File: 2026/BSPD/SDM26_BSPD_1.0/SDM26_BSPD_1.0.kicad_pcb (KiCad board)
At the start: 2 copper layers, 10 parts, among them Q1 2N7002,215, Q2 2N7002,215

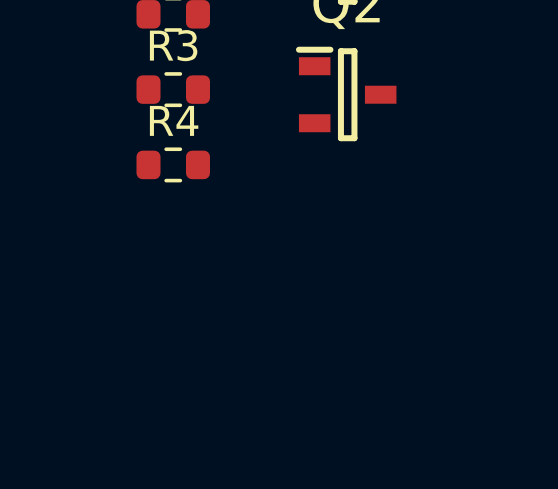
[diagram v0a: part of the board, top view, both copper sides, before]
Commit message: BSPD logic and latch simulated in Falstad
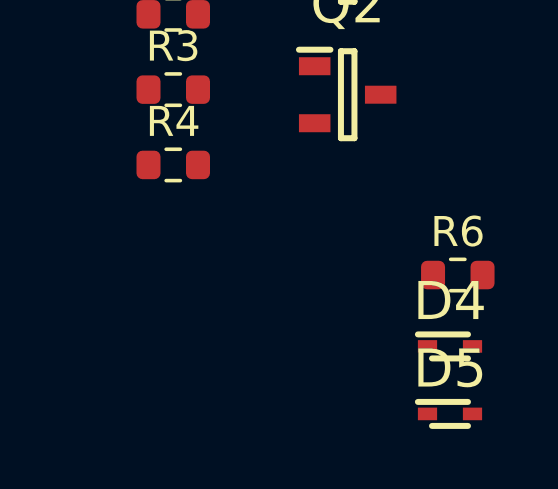
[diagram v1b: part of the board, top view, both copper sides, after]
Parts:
- added D4: BAT54XV2T1G, SDM_MiscFootprint:SODFL1608X70N, F.Cu at (125.5, 93.8)
- added D5: BAT54XV2T1G, SDM_MiscFootprint:SODFL1608X70N, F.Cu at (125.5, 96.0)
- added R6: 1k, Resistor_SMD:R_0603_1608Metric, F.Cu at (125.8, 91.4)
- D1, D2: footprint SDM_DIODE:SODFL1608X70N -> SDM_MiscFootprint:SODFL1608X70N
- D3: footprint SDM_SCR:SOT230P700X190-4N -> SDM_MiscFootprint:SOT230P700X190-4N
- Q1: footprint SDM_MOSFET_N-CHANNEL:SOT95P230X110-3N -> SDM_MiscFootprint:SOT95P230X110-3N
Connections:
- D1 pad 1: Net-(D1-K) -> /SCR Gate
- D3 pad 1: GND -> (no net)
- D3 pad 2: BSPD SIGNAL OUT -> (no net)
- D3 pad 3: Net-(D1-K) -> (no net)
- D3 pad 4: BSPD SIGNAL OUT -> (no net)
- Q1 pad 1: /12V MASTER -> (no net)
- Q1 pad 2: GND -> (no net)
- Q1 pad 3: Net-(D1-A) -> (no net)
- R1 pad 1: Net-(D1-A) -> /12V IGNITION
- R1 pad 2: /12V IGNITION -> Net-(D1-A)
- R2 pad 1: Net-(D1-K) -> /SCR Gate
- R4 pad 1: /12V IGNITION -> Net-(D4-K)
- R4 pad 2: BSPD SIGNAL OUT -> BSPD KILL SIGNAL

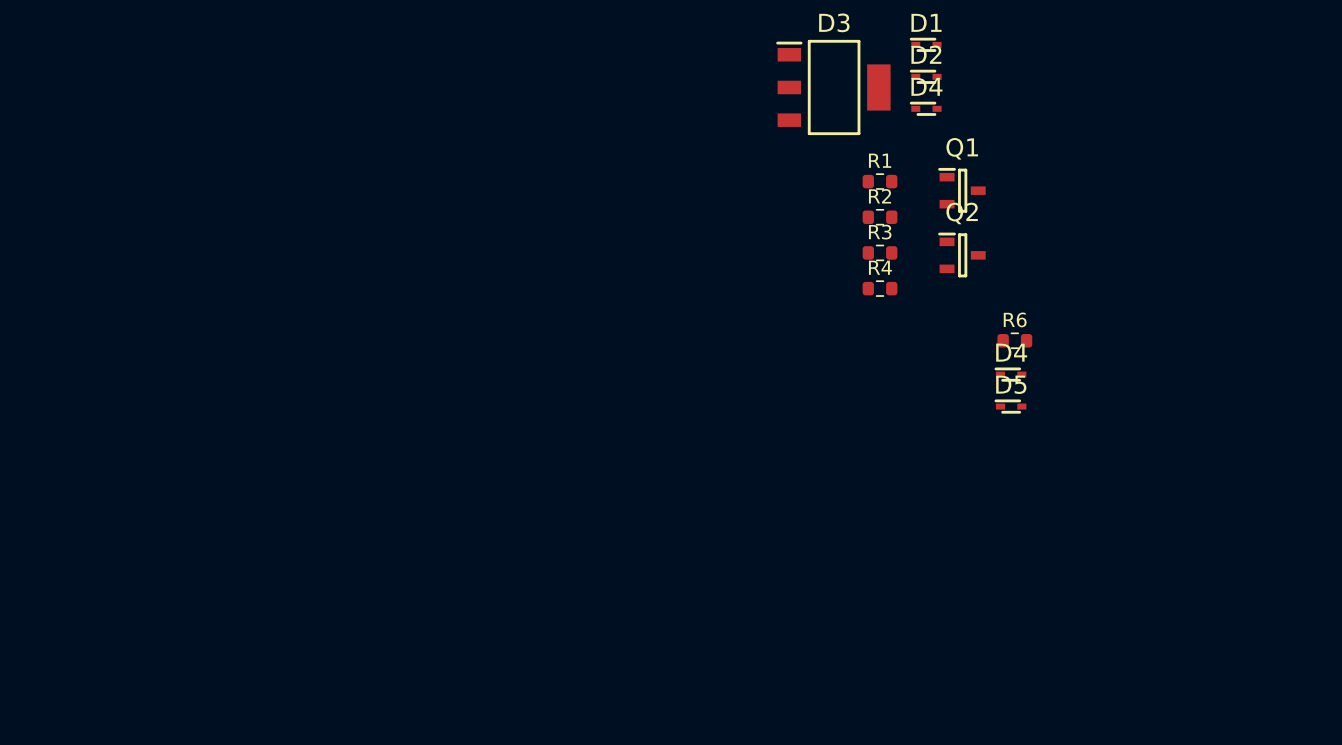
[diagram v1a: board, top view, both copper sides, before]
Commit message: BSPD power regulation + Splitter format changes
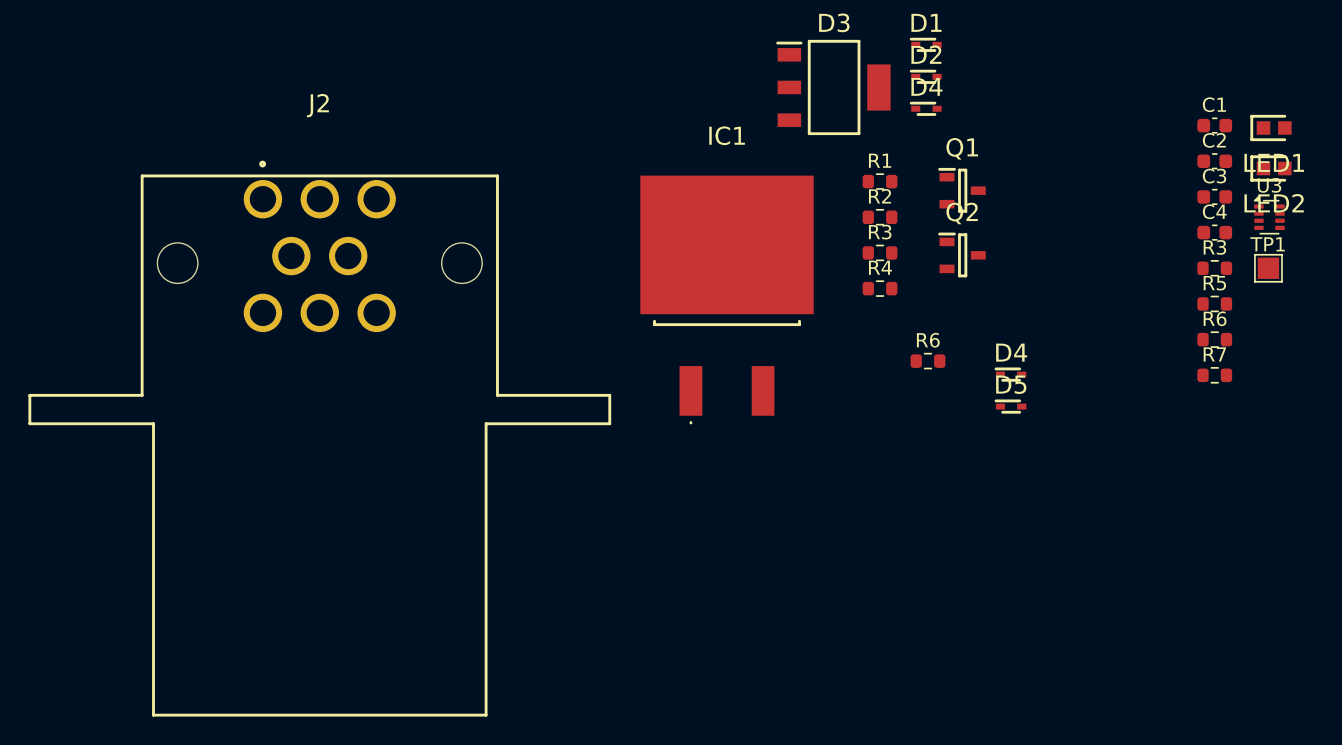
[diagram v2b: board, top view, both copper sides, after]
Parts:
- added C1: 0.1uF, Capacitor_SMD:C_0603_1608Metric, F.Cu at (139.9, 76.2)
- added C2: 0.33uF, Capacitor_SMD:C_0603_1608Metric, F.Cu at (139.9, 78.7)
- added C3: 1uF, Capacitor_SMD:C_0603_1608Metric, F.Cu at (139.9, 81.2)
- added C4: 1uF, Capacitor_SMD:C_0603_1608Metric, F.Cu at (139.9, 83.8)
- added IC1: L7805ACD2T-TR, SDM_MiscFootprint:L7805ACD2TTR, F.Cu at (105.6, 88.0)
- added J2: 776280-1, SDM_MiscFootprint:776280-1, F.Cu at (76.9, 97.2)
- added LED1: 150060RS75000, SDM_MiscFootprint:LEDC1608X80N, F.Cu at (144.1, 76.4)
- added LED2: 150060RS75000, SDM_MiscFootprint:LEDC1608X80N, F.Cu at (144.1, 79.2)
- added R3: 220, Resistor_SMD:R_0603_1608Metric, F.Cu at (139.9, 86.3)
- added R5: 10k, Resistor_SMD:R_0603_1608Metric, F.Cu at (139.9, 88.8)
- added R6: 10k, Resistor_SMD:R_0603_1608Metric, F.Cu at (139.9, 91.3)
- added R7: 10k, Resistor_SMD:R_0603_1608Metric, F.Cu at (139.9, 93.8)
- added TP1: ST_5V, TestPoint:TestPoint_Pad_1.5x1.5mm, F.Cu at (143.7, 86.3)
- added U3: TPS2116DRL, Package_TO_SOT_SMD:SOT-583-8, F.Cu at (143.7, 82.7)
- D4: footprint SDM_DIODE:SODFL1608X70N -> SDM_MiscFootprint:SODFL1608X70N
- Q2: footprint SDM_MOSFET_N-CHANNEL:SOT95P230X110-3N -> SDM_MiscFootprint:SOT95P230X110-3N
- R2: value 10k -> 1k
- R4: value 1k -> 470
- moved R6 6.28 mm to (119.7, 92.8)
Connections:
- D3 pad 1: (no net) -> GND
- D3 pad 2: (no net) -> BSPD KILL SIGNAL
- D3 pad 3: (no net) -> /SCR Gate
- D3 pad 4: (no net) -> BSPD KILL SIGNAL
- Q1 pad 1: (no net) -> /12V MASTER
- Q1 pad 2: (no net) -> GND
- Q1 pad 3: (no net) -> Net-(D1-A)
- R4 pad 2: BSPD KILL SIGNAL -> Net-(LED1-A)

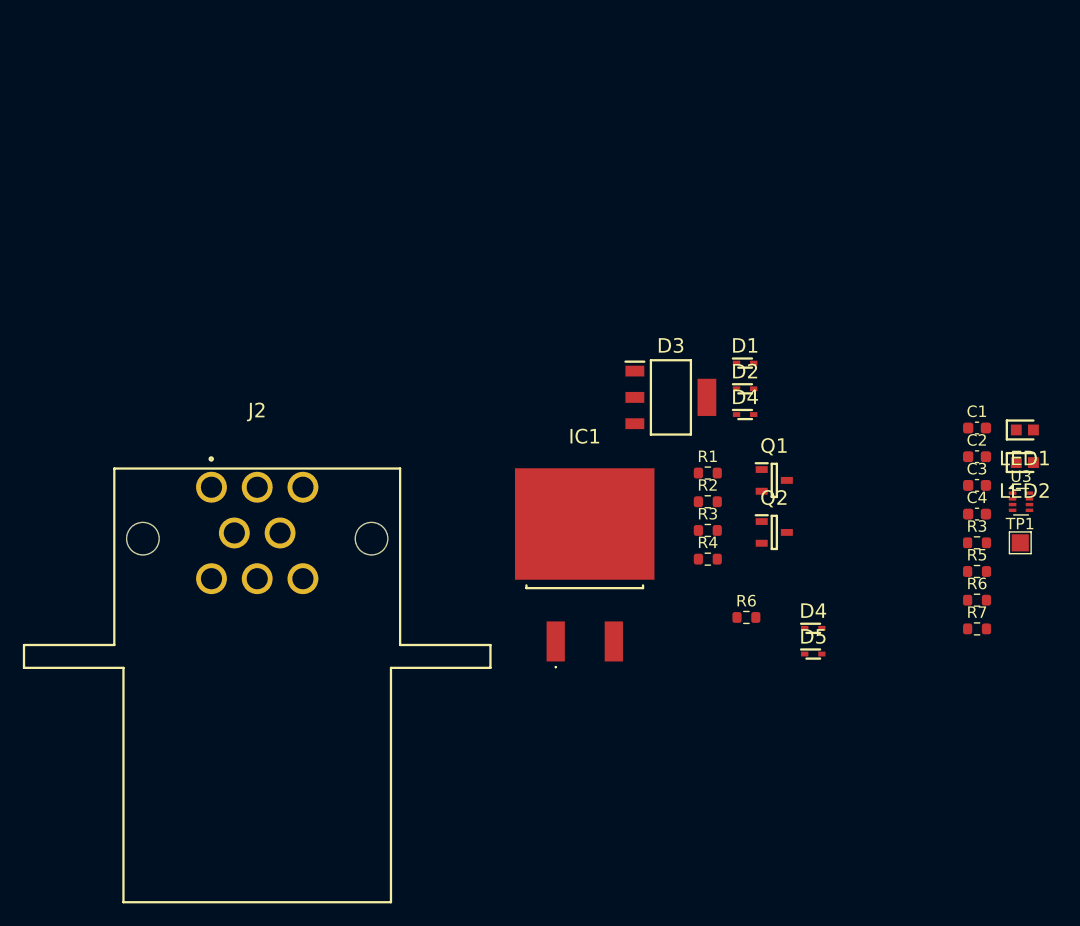
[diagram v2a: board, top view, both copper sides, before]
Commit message: BSPD Schematic mostly done
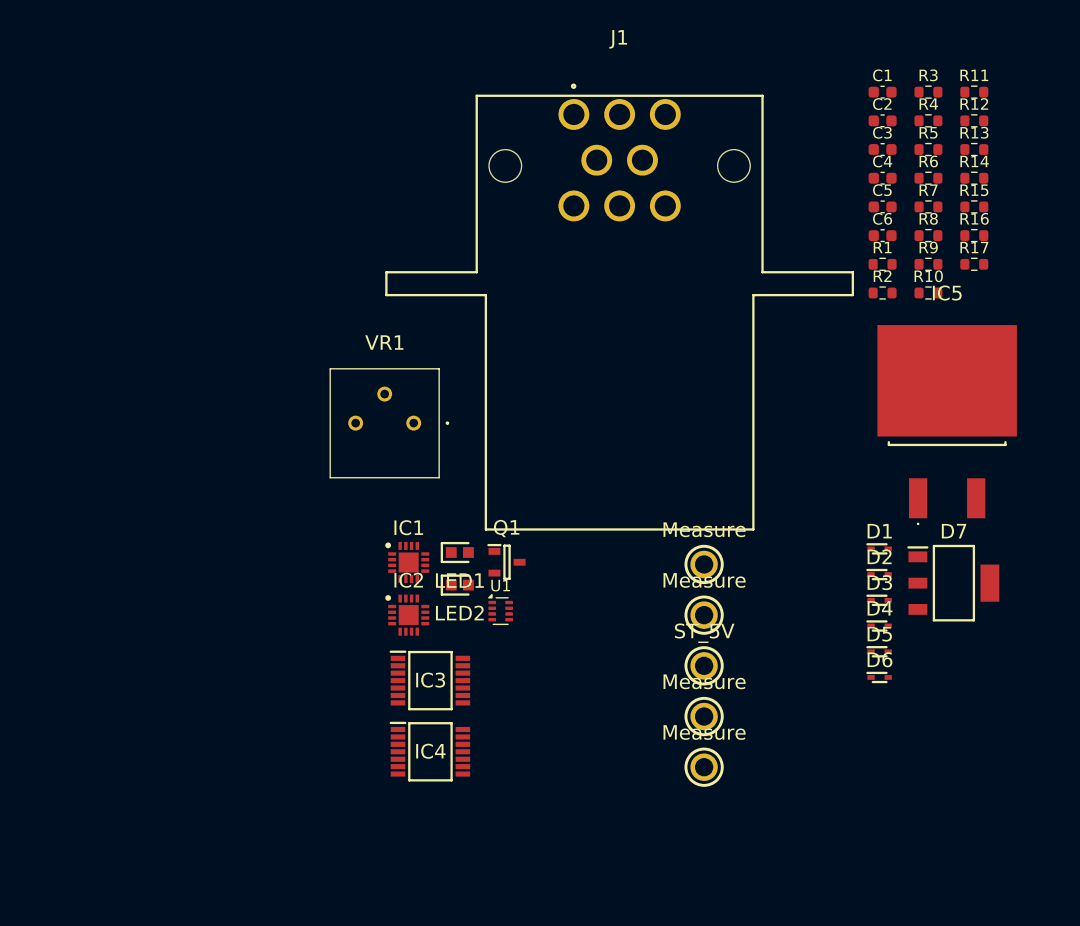
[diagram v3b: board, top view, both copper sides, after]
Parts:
- removed the D4 at (125.5, 93.8)
- removed the D4 at (119.6, 75.0)
- removed J2: 776280-1, SDM_MiscFootprint:776280-1
- removed Q2: 2N7002,215, SDM_MiscFootprint:SOT95P230X110-3N
- removed the R3 at (116.3, 85.2)
- removed the R3 at (139.9, 86.3)
- removed the R6 at (139.9, 91.3)
- removed the R6 at (119.7, 92.8)
- removed TP1: ST_5V, TestPoint:TestPoint_Pad_1.5x1.5mm
- removed U3: TPS2116DRL, Package_TO_SOT_SMD:SOT-583-8
- added BLACK_TP1: 5006, SDM_MiscFootprint:5006, F.Cu at (116.0, 88.2)
- added C5: 1uF, Capacitor_SMD:C_0603_1608Metric, F.Cu at (131.6, 56.9)
- added C6: 1uF, Capacitor_SMD:C_0603_1608Metric, F.Cu at (131.6, 59.4)
- added D4: BAT54XV2T1G, SDM_MiscFootprint:SODFL1608X70N, F.Cu at (131.4, 93.5)
- added D6: BAT54XV2T1G, SDM_MiscFootprint:SODFL1608X70N, F.Cu at (131.4, 98.0)
- added D7: X0202MN_5BA4, SDM_MiscFootprint:SOT230P700X190-4N, F.Cu at (137.8, 89.8)
- added IC2: LM2901BIRTER, SDM_MiscFootprint:QFN50P300X300X80-17L-D, F.Cu at (90.2, 92.6)
- added IC3: SN74HC08PWR, SDM_MiscFootprint:SOP65P640X120-14L, F.Cu at (92.1, 98.3)
- added IC4: SN74HC32PWR, SDM_MiscFootprint:SOP65P640X120-14L, F.Cu at (92.1, 104.5)
- added IC5: L7805ACD2T-TR, SDM_MiscFootprint:L7805ACD2TTR, F.Cu at (137.3, 75.5)
- added J1: 776280-1, SDM_MiscFootprint:776280-1, F.Cu at (108.6, 64.6)
- added ORANGE_TP1: 5008, SDM_MiscFootprint:5008, F.Cu at (116.0, 92.6)
- added R10: 100, Resistor_SMD:R_0603_1608Metric, F.Cu at (135.6, 64.4)
- added R11: 10k, Resistor_SMD:R_0603_1608Metric, F.Cu at (139.6, 46.9)
- added R12: 470, Resistor_SMD:R_0603_1608Metric, F.Cu at (139.6, 49.4)
- added R13: 1k, Resistor_SMD:R_0603_1608Metric, F.Cu at (139.6, 51.9)
- added R14: 10k, Resistor_SMD:R_0603_1608Metric, F.Cu at (139.6, 54.4)
- added R15: 220, Resistor_SMD:R_0603_1608Metric, F.Cu at (139.6, 56.9)
- added R16: 10k, Resistor_SMD:R_0603_1608Metric, F.Cu at (139.6, 59.4)
- added R17: 10k, Resistor_SMD:R_0603_1608Metric, F.Cu at (139.6, 61.9)
- added R3: 10k, Resistor_SMD:R_0603_1608Metric, F.Cu at (135.6, 46.9)
- added R6: 10k, Resistor_SMD:R_0603_1608Metric, F.Cu at (135.6, 54.4)
- added R8: 100, Resistor_SMD:R_0603_1608Metric, F.Cu at (135.6, 59.4)
- added R9: 10k, Resistor_SMD:R_0603_1608Metric, F.Cu at (135.6, 61.9)
- added RED_TP1: 5005, SDM_MiscFootprint:5005, F.Cu at (116.0, 97.0)
- added U1: TPS2116DRL, Package_TO_SOT_SMD:SOT-583-8, F.Cu at (98.2, 92.2)
- added VR1: 3386P-1-103TLF, SDM_MiscFootprint:3386P1103TLF, F.Cu at (90.6, 75.8)
- added WHITE_TP1: 5007, SDM_MiscFootprint:5007, F.Cu at (116.0, 101.5)
- added YELLOW_TP1: 5009, SDM_MiscFootprint:5009, F.Cu at (116.0, 105.9)
- C1: value 0.1uF -> 10uF
- C2: value 0.33uF -> 10uF
- C3: value 1uF -> 0.33uF
- C4: value 1uF -> 0.1uF
- D3: value X0202MN_5BA4 -> BAT54XV2T1G; footprint SDM_MiscFootprint:SOT230P700X190-4N -> SDM_MiscFootprint:SODFL1608X70N
- IC1: value L7805ACD2T-TR -> LM2901BIRTER; footprint SDM_MiscFootprint:L7805ACD2TTR -> SDM_MiscFootprint:QFN50P300X300X80-17L-D
- R2: value 1k -> 10k
- R4: value 470 -> 10k
- R7: value 10k -> 100k
- moved LED1 50.6 mm to (94.6, 87.1)
- moved LED2 50.6 mm to (94.6, 90.0)
- moved R4 42.9 mm to (135.6, 49.4)
- moved R5 37.2 mm to (135.6, 51.9)
- moved R7 37.2 mm to (135.6, 56.9)
- moved C1 30.5 mm to (131.6, 46.9)
- moved C2 30.5 mm to (131.6, 49.4)
- moved C3 30.5 mm to (131.6, 51.9)
- moved C4 30.5 mm to (131.6, 54.4)
- moved D3 25.5 mm to (131.4, 91.3)
- moved Q1 24.5 mm to (98.8, 88.0)
- moved R1 23.8 mm to (131.6, 61.9)
- moved R2 23.8 mm to (131.6, 64.4)
- moved D1 20.1 mm to (131.4, 86.8)
- moved D2 20.1 mm to (131.4, 89.0)
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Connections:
- C1 pad 1: GND -> /HB*T10_FAULT
- C1 pad 2: /5V IGNITION -> GND
- C2 pad 1: GND -> /BL+TL+(HB*T10)_FAULT
- C2 pad 2: /12V IGNITION -> GND
- C3 pad 1: /5V IGNITION -> GND
- C3 pad 2: GND -> /12V IGNITION
- C4 pad 1: /5V PDM -> GND
- C4 pad 2: GND -> /5V IGNITION
- D1 pad 1: /SCR Gate -> Net-(D1-K)
- D1 pad 2: Net-(D1-A) -> /HB*T10_FAULT
- D2 pad 2: /BSPD LOGIC SIGNAL -> /BL+TL+(HB*T10)_FAULT
- D3 pad 1: GND -> Net-(D3-K)
- D3 pad 2: BSPD KILL SIGNAL -> /12V IGNITION
- D5 pad 1: Net-(D4-K) -> /SCR Gate
- D5 pad 2: /12V MASTER -> Net-(D5-A)
- IC1 pad 1: /12V IGNITION -> +5V
- IC1 pad 2: GND -> /BRAKE_LOW_REF
- IC1 pad 3: /5V IGNITION -> unconnected-(IC1-NC_1-Pad3)
- Q1 pad 3: Net-(D1-A) -> Net-(D5-A)
- R1 pad 1: /12V IGNITION -> +5V
- R1 pad 2: Net-(D1-A) -> /BREAK_LOW_FAULT
- R2 pad 1: /SCR Gate -> +5V
- R2 pad 2: Net-(D2-K) -> /HEAVY_BREAKING_FAULT
- R4 pad 1: Net-(D4-K) -> +5V
- R4 pad 2: Net-(LED1-A) -> /TPS_LOW_FAULT
- R5 pad 1: /5V PDM -> +5V
- R5 pad 2: Net-(U3-PR1) -> /HB*T10_1S_FAULT
- R7 pad 1: +5V -> Net-(IC3-2Y)
- R7 pad 2: Net-(U3-ST) -> /HB*T10_FAULT
